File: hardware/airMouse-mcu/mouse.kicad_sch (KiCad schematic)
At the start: 40 parts, among them SW50 KEY, SW51 KEY, SW52 KEY, SW53 KEY, SW54 KEY, SW55 KEY, SW56 KEY, SW57 KEY, SW58 KEY, SW59 KEY

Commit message: add mouse pcb
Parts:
- removed R26, R27, R28, R38, R39, R40, R41, R42, R43, R45: 10k, Resistor_SMD:R_0603_1608Metric, symbol Device:R
- removed SW50, SW51, SW52, SW53, SW54, SW55, SW56, SW57, SW58, SW59: KEY, airMouseLib:TL3315NF100Q, symbol airMouseLib:KEY
- added J5: DS1020-07-10VBT1A-R, airMouseLib:DS1020-07-10VBT1A-R, symbol Connector_Generic_MountingPin:Conn_01x10_MountingPin
- added J6: Conn_01x04_MountingPin, airMouseLib:DS1020-07-4VBT1A-R, symbol Connector_Generic_MountingPin:Conn_01x04_MountingPin
- renumbered C25 to C26, C24 to C27, C23 to C28, C22 to C29, C21 to C30, C20 to C31, C19 to C32, C16 to C33, C17 to C34, C18 to C35, R29 to R43, R30 to R44, R31 to R45, R32 to R46, R33 to R47, R34 to R48, R35 to R49, R36 to R50, R37 to R51, R44 to R52
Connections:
- net +3V3: now also J5.10 (Pin_10), J6.4 (Pin_4)
- net BACK: now also R52.1, J6.2 (Pin_2); no longer R49.1
- net DPI: now also R48.1, J5.4 (Pin_4); no longer R50.1
- net FWD: now also R51.1, J6.3 (Pin_3); no longer R48.1
- net GND: now also J5.1 (Pin_1), J5.MP (MountPin), J6.1 (Pin_1), J6.MP (MountPin)
- net HOME: now also R50.1, J5.2 (Pin_2); no longer R52.1
- net LMB: now also J5.9 (Pin_9)
- net MMB: now also J5.8 (Pin_8)
- net PRECISION: now also R49.1, J5.3 (Pin_3); no longer R51.1
- net RMB: now also J5.7 (Pin_7)
- net SCRLDN: now also J5.5 (Pin_5)
- net SCRLUP: now also J5.6 (Pin_6)
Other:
- note removed: "keys: TL3315NF100Q"

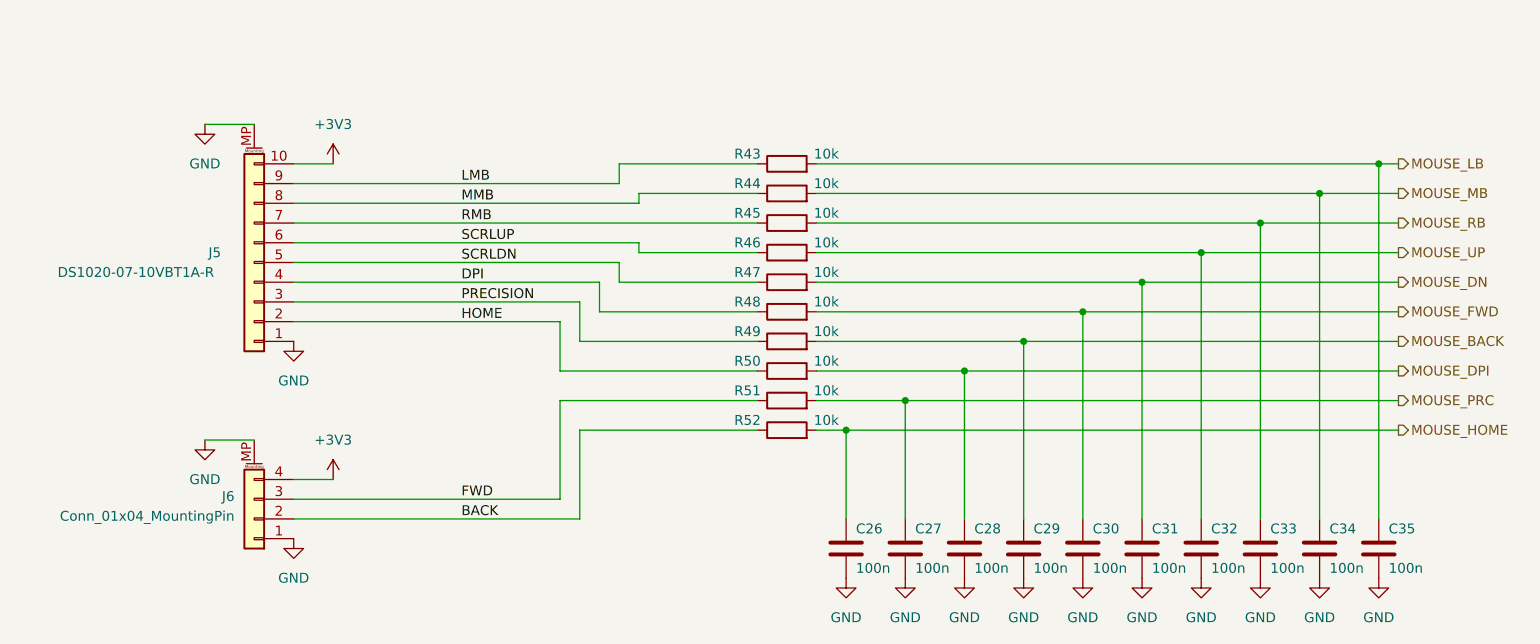
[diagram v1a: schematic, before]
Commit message: components placed on mcu board
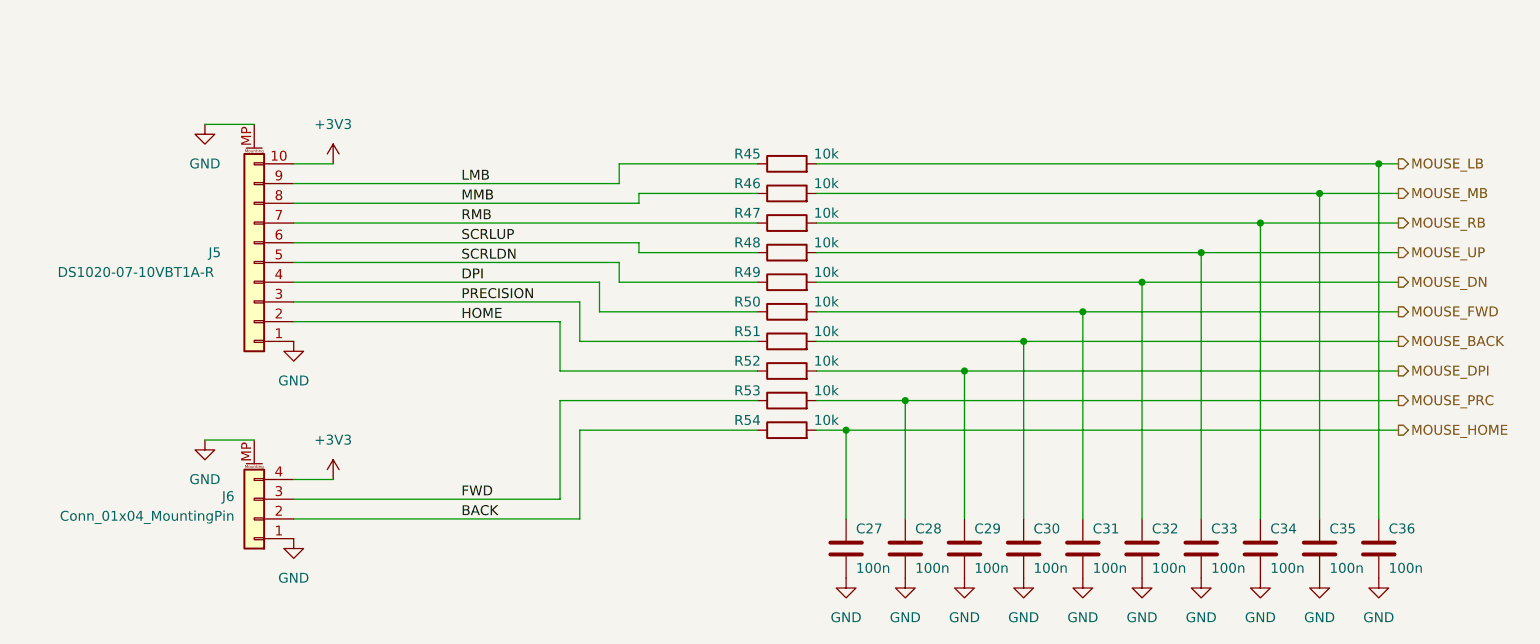
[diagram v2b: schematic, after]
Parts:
- renumbered C26 to C27, C27 to C28, C28 to C29, C29 to C30, C30 to C31, C31 to C32, C32 to C33, C33 to C34, C34 to C35, C35 to C36, R43 to R45, R44 to R46, R45 to R47, R46 to R48, R47 to R49, R48 to R50, R49 to R51, R50 to R52, R51 to R53, R52 to R54

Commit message: add mcu board
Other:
- title: EtherPointer -> EtherPointer mcu
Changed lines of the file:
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@@
 	(paper "A4")
 	(title_block
-		(title "EtherPointer")
-		(date "2025-02-13")
+		(title "EtherPointer mcu")
+		(date "2025-02-15")
 		(rev "RC1")
 		(company "Bart's Design")

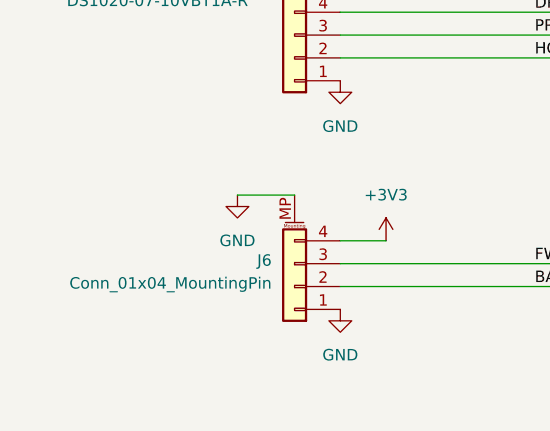
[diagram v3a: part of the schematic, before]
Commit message: add connectors 3d models
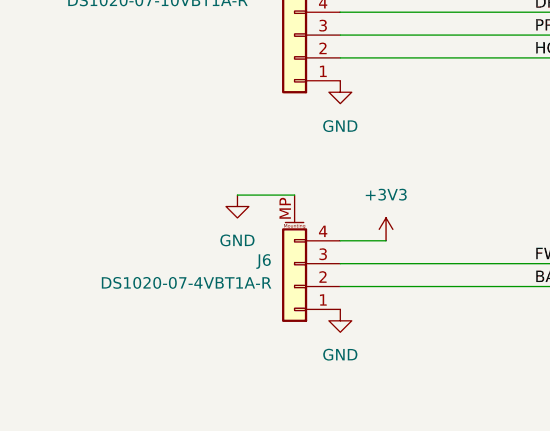
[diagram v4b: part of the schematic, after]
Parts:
- J6: value Conn_01x04_MountingPin -> DS1020-07-4VBT1A-R
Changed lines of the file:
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@@
 (kicad_sch
-	(version 20231120)
+	(version 20250114)
 	(generator "eeschema")
-	(generator_version "8.0")
+	(generator_version "9.0")
 	(paper "A4")
 	(title_block
@@
 	(label "RMB"
 		(at 82.55 69.85 0)
-		(fields_autoplaced yes)
 		(effects
 			(font
@@
 	(label "DPI"
 		(at 82.55 77.47 0)
-		(fields_autoplaced yes)
 		(effects
 			(font
@@
 	(label "HOME"
 		(at 82.55 82.55 0)
-		(fields_autoplaced yes)
 		(effects
 			(font
@@
 	(label "PRECISION"
 		(at 82.55 80.01 0)
-		(fields_autoplaced yes)
 		(effects
 			(font
@@
 	(label "BACK"
 		(at 82.55 107.95 0)
-		(fields_autoplaced yes)
 		(effects
 			(font
@@
 	(label "MMB"
 		(at 82.55 67.31 0)
-		(fields_autoplaced yes)
 		(effects
 			(font
@@
 	(label "SCRLDN"
 		(at 82.55 74.93 0)
-		(fields_autoplaced yes)
 		(effects
 			(font
@@
 	(label "SCRLUP"
 		(at 82.55 72.39 0)
-		(fields_autoplaced yes)
 		(effects
 			(font
@@
 	(label "FWD"
 		(at 82.55 105.41 0)
-		(fields_autoplaced yes)
 		(effects
 			(font
@@
 	(label "LMB"
 		(at 82.55 64.77 0)
-		(fields_autoplaced yes)
 		(effects
 			(font
@@
 		(shape output)
 		(at 203.2 85.09 0)
-		(fields_autoplaced yes)
 		(effects
 			(font
@@
 		(shape output)
 		(at 203.2 92.71 0)
-		(fields_autoplaced yes)
 		(effects
 			(font
@@
 		(shape output)
 		(at 203.2 81.28 0)
-		(fields_autoplaced yes)
 		(effects
 			(font
@@
 		(shape output)
 		(at 203.2 96.52 0)
-		(fields_autoplaced yes)
 		(effects
 			(font
@@
 		(shape output)
 		(at 203.2 88.9 0)
-		(fields_autoplaced yes)
 		(effects
 			(font
@@
 		(shape output)
 		(at 203.2 73.66 0)
-		(fields_autoplaced yes)
 		(effects
 			(font
@@
 		(shape output)
 		(at 203.2 69.85 0)
-		(fields_autoplaced yes)
 		(effects
 			(font
@@
 		(shape output)
 		(at 203.2 66.04 0)
-		(fields_autoplaced yes)
 		(effects
 			(font
@@
 		(shape output)
 		(at 203.2 62.23 0)
-		(fields_autoplaced yes)
 		(effects
 			(font
@@
 		(shape output)
 		(at 203.2 77.47 0)
-		(fields_autoplaced yes)
 		(effects
 			(font
@@
 			)
 		)
-		(property "Value" "Conn_01x04_MountingPin"
+		(property "Value" "DS1020-07-4VBT1A-R"
 			(at 53.34 107.5943 0)
 			(effects

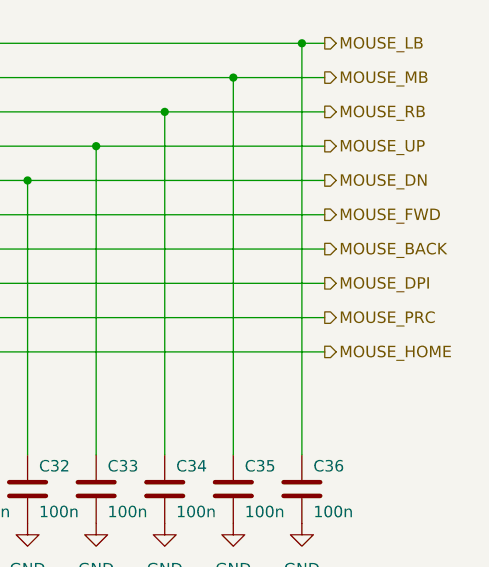
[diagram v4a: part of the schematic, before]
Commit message: fixed home/prc and fwd/bck
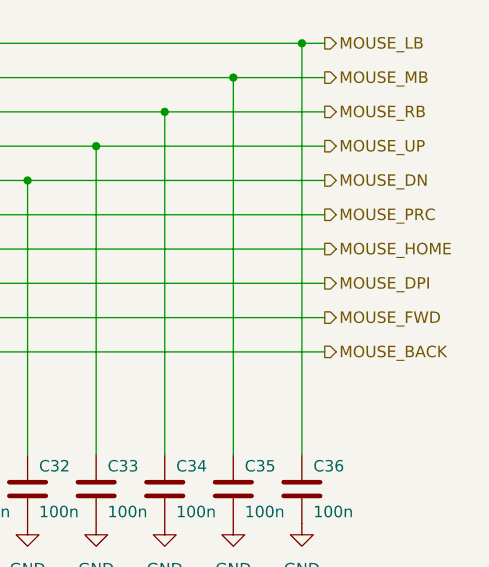
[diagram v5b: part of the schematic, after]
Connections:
- net MOUSE_BACK: now also C27.1, R54.2; no longer C30.1, R51.2
- net MOUSE_FWD: now also C28.1, R53.2; no longer C31.1, R50.2
- net MOUSE_HOME: now also C30.1, R51.2; no longer C27.1, R54.2
- net MOUSE_PRC: now also C31.1, R50.2; no longer C28.1, R53.2
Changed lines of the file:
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@@
 		)
 	)
-	(hierarchical_label "MOUSE_BACK"
+	(hierarchical_label "MOUSE_HOME"
 		(shape output)
 		(at 203.2 85.09 0)
@@
 		)
 	)
-	(hierarchical_label "MOUSE_PRC"
+	(hierarchical_label "MOUSE_FWD"
 		(shape output)
 		(at 203.2 92.71 0)
@@
 		)
 	)
-	(hierarchical_label "MOUSE_FWD"
+	(hierarchical_label "MOUSE_PRC"
 		(shape output)
 		(at 203.2 81.28 0)
@@
 		)
 	)
-	(hierarchical_label "MOUSE_HOME"
+	(hierarchical_label "MOUSE_BACK"
 		(shape output)
 		(at 203.2 96.52 0)

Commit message: new mcu pcb
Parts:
- removed C27, C28, C29, C30, C31, C32, C33, C34, C35, C36: 100n, Capacitor_SMD:C_0603_1608Metric, symbol Device:C
- removed R45, R46, R47, R48, R49, R50, R51, R52, R53, R54: 10k, Resistor_SMD:R_0603_1608Metric, symbol Device:R
- added C8: 100n, Capacitor_SMD:C_0603_1608Metric, symbol Device:C
- added R25: 10k, Resistor_SMD:R_0603_1608Metric, symbol Device:R
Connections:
- net BACK is gone; now on net MOUSE_BACK: J6.2 (Pin_2)
- net DPI is gone; now on net MOUSE_PRC: J5.4 (Pin_4)
- net FWD is gone; now on net MOUSE_FWD: J6.3 (Pin_3)
- net HOME is gone; now on net MOUSE_DPI: J5.2 (Pin_2)
- net MMB is gone; now on net MOUSE_MB: J5.8 (Pin_8)
- net PRECISION is gone; now on net MOUSE_HOME: J5.3 (Pin_3)
- net RMB is gone; now on net MOUSE_RB: J5.7 (Pin_7)
- net SCRLDN is gone; now on net MOUSE_DN: J5.5 (Pin_5)
- net SCRLUP is gone; now on net MOUSE_UP: J5.6 (Pin_6)
- net GND: now also C8.2
- net MOUSE_LB: now also C8.1, R25.2
- net LMB: no longer names the net of J5.9 (Pin_9)
- net LMB: now also R25.1

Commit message: new mcu-pcb
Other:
- title: EtherPointer mcu -> Neuro Glider
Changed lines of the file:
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@@
 	(paper "A4")
 	(title_block
-		(title "EtherPointer mcu")
-		(date "2025-02-15")
-		(rev "RC1")
+		(title "Neuro Glider")
+		(date "2025-03-21")
+		(rev "v1.0")
 		(company "Bart's Design")
 		(comment 1 "Bartosz Pracz")
